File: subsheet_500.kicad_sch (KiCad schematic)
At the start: 48 parts, among them J500 DM-15S — JOY0, J501 DM-15S — JOY1, U513 LM556_DUAL_TIMER_PHY, U514 LM556_DUAL_TIMER_PHY

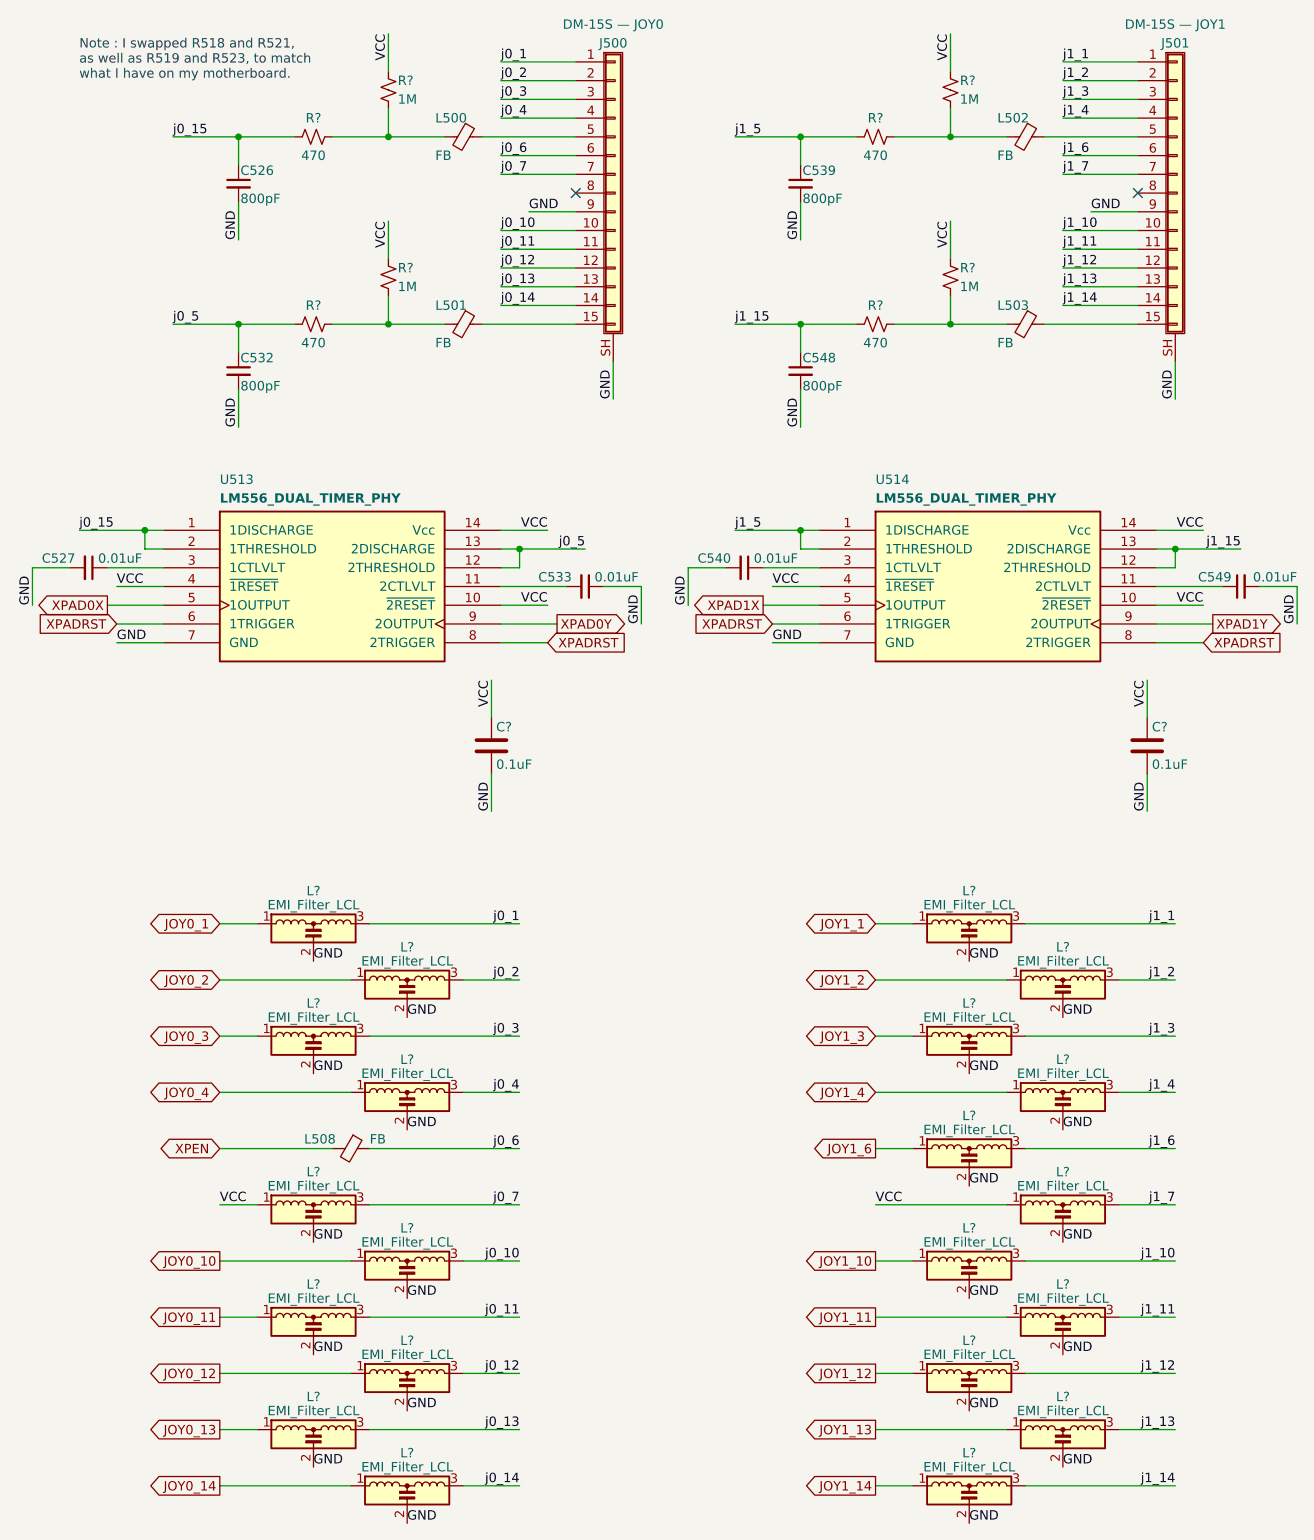
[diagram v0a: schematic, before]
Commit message: Resolves #3 : [schematic] annotate video port with signal name
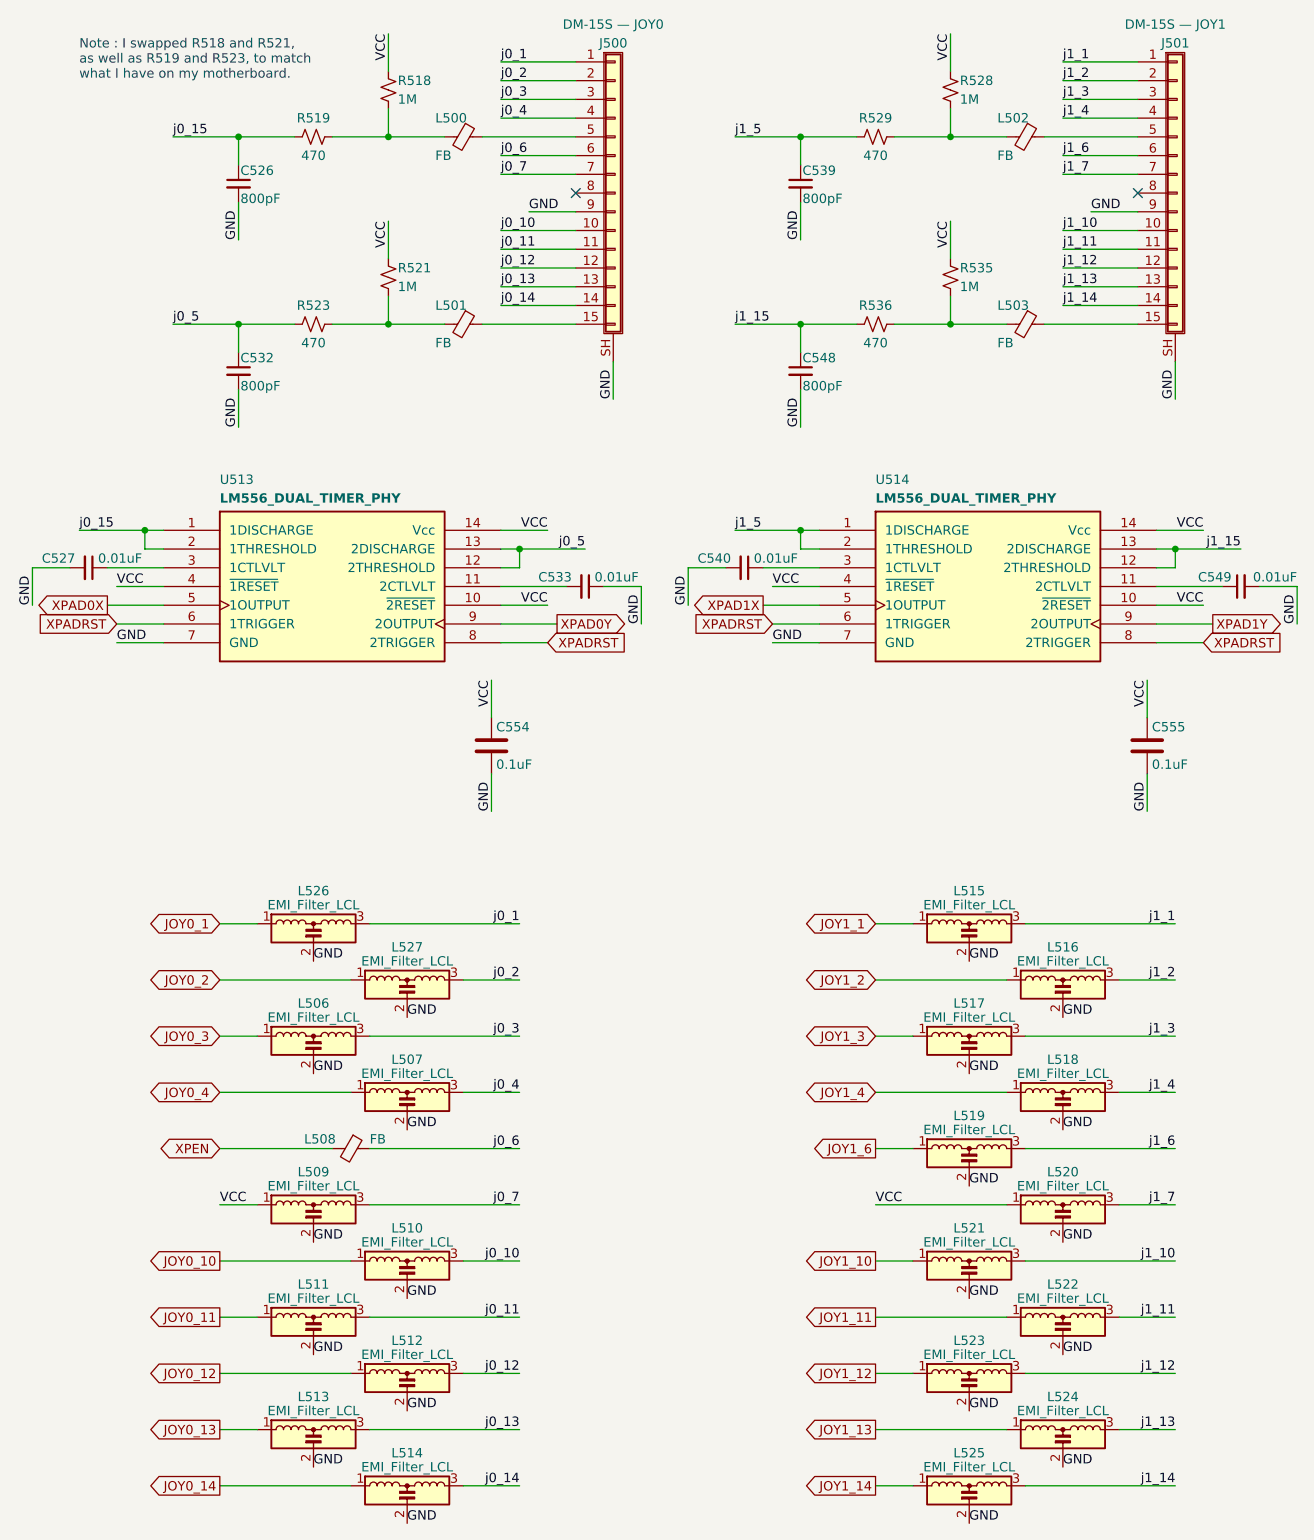
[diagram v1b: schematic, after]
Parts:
- gave numbers to parts that had none: 31
